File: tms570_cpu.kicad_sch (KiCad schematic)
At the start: 49 parts, among them J12 TS-103-G-A, J3 FTSH-105-01-L-DV-K, U2 TMS5700914APGEQQ1

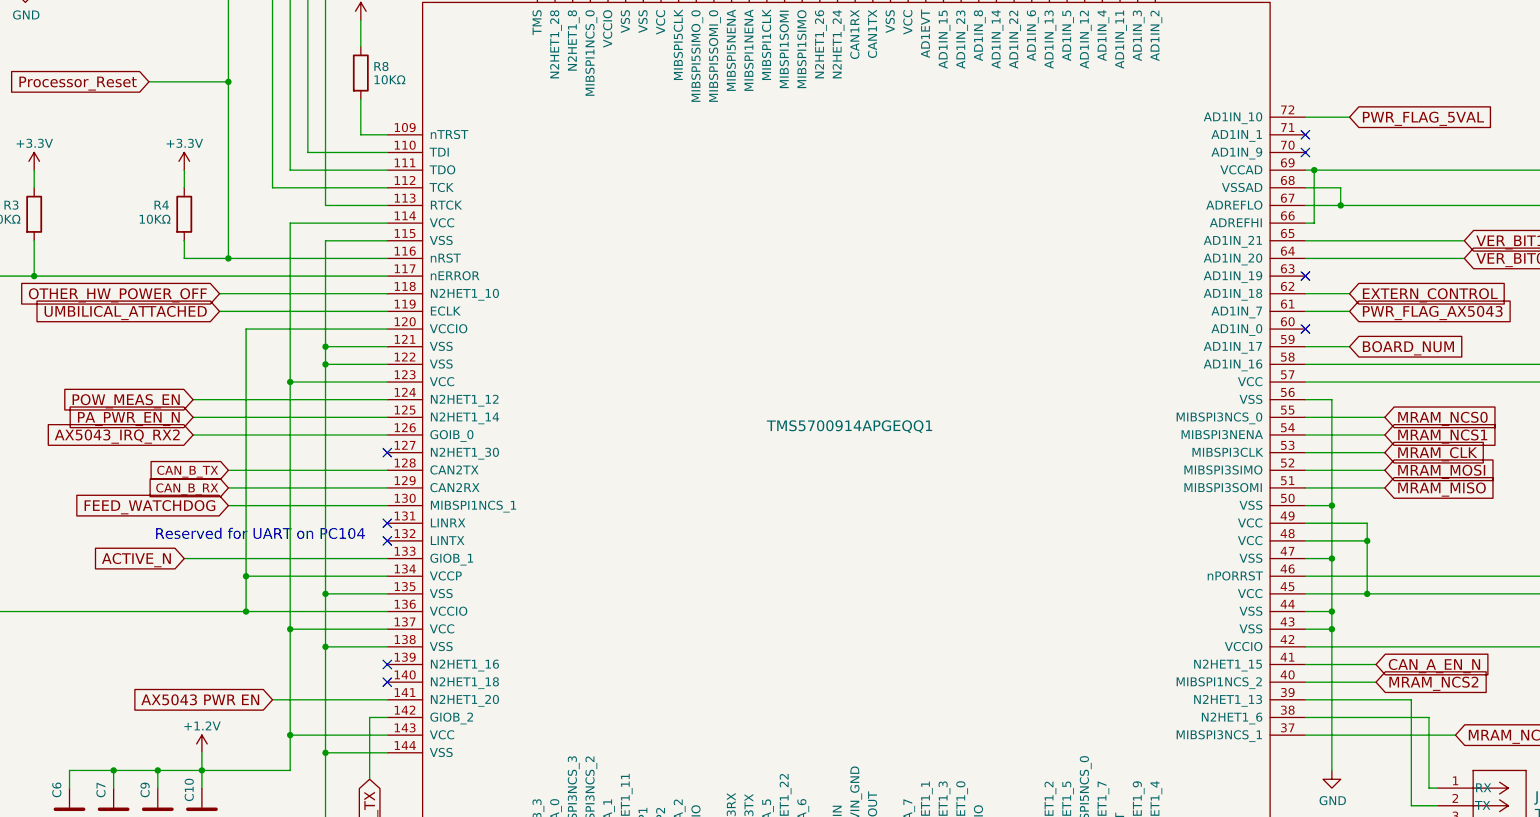
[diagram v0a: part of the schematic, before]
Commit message: Add some signals to the PC104
Add DNP zero-ohm resistors on the I2C lines to the PC104 so they can
be disconnected.

Add UART lines to the PC104 connected via DNP zero-ohm resistors.

Add a way to measure battery voltage from the PC104, currently with
DNP zero ohm resistors.

Signed-off-by: Corey Minyard <corey@minyard.net>
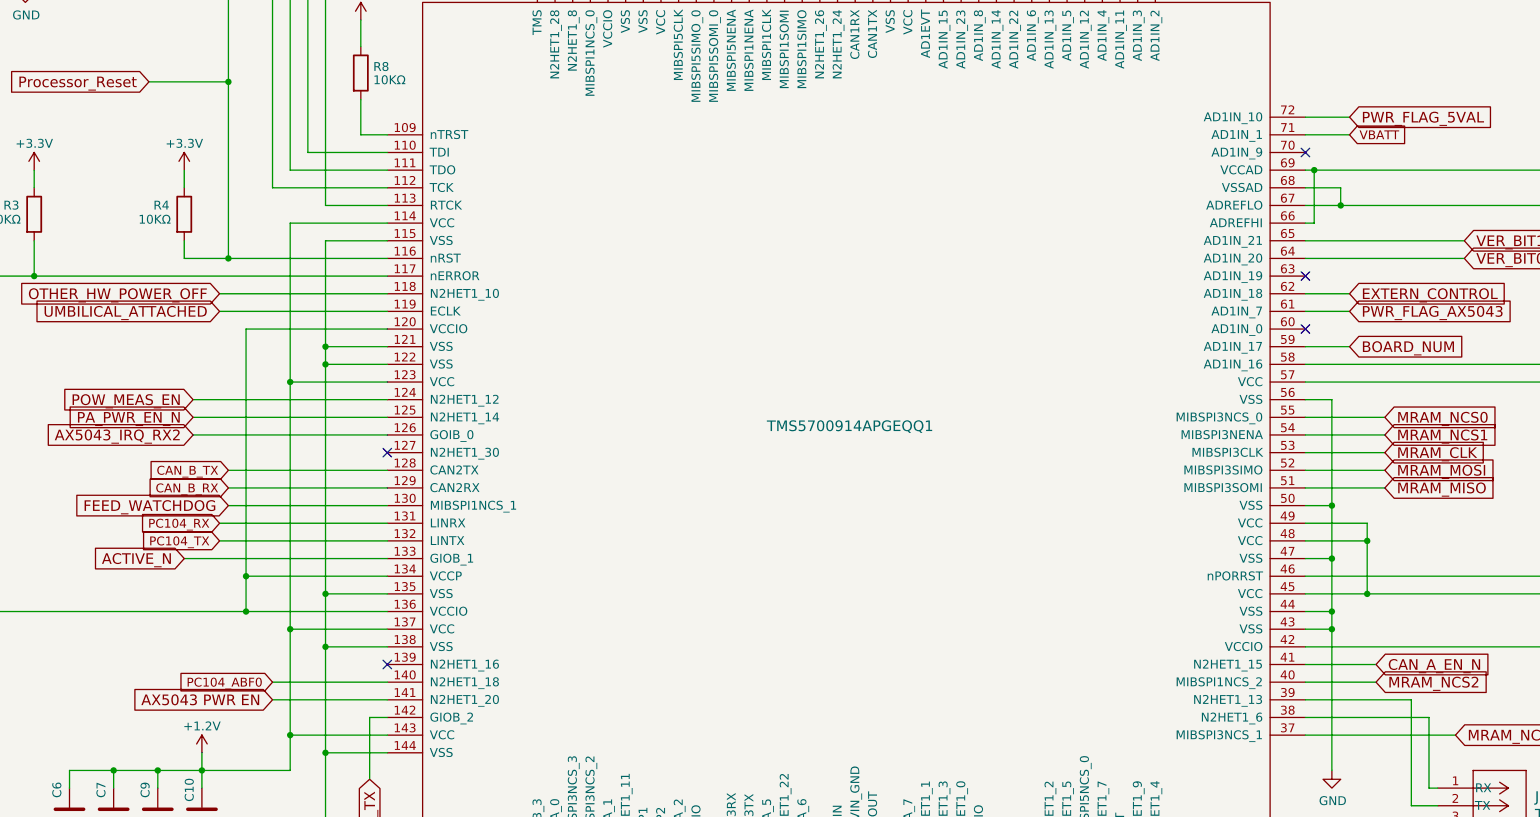
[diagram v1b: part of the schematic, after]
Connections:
- net PC104_RX: now reaches U2.131 (LINRX)
- net PC104_TX: now reaches U2.132 (LINTX)
- net PC104_ABF0: now reaches U2.140 (N2HET1_18)
- net VBATT: now reaches U2.71 (AD1IN_1)
- no-connect marks 22 -> 18
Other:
- note removed: "Reserved for UART on PC104"
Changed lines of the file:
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@@
 		)
 	)
-	(text "Reserved for UART on PC104"
-		(exclude_from_sim no)
-		(at 131.572 154.178 0)
-		(effects
-			(font
-				(size 1.524 1.524)
-			)
-		)
-	)
 	(text "Thermsistor varies from 534\nohms (125C) to 188.5KΩ (-40C).\nWith a 10KΩ bias this gives a\n.17 to 3.13V range."
 		(exclude_from_sim no)
@@
 	)
 	(no_connect
-		(at 281.94 96.52)
-	)
-	(no_connect
 		(at 281.94 124.46)
 	)
 	(no_connect
-		(at 149.86 154.94)
-	)
-	(no_connect
 		(at 196.85 72.39)
 	)
@@
 	)
 	(no_connect
-		(at 149.86 175.26)
-	)
-	(no_connect
-		(at 149.86 152.4)
-	)
-	(no_connect
 		(at 149.86 142.24)
 	)
@@
 	)
 	(no_connect
-		(at 281.94 99.06)
-	)
-	(no_connect
 		(at 191.77 72.39)
 	)
@@
 	)
 	(no_connect
+		(at 281.94 99.06)
+	)
+	(no_connect
 		(at 176.53 72.39)
 	)
@@
 	(wire
 		(pts
+			(xy 281.94 96.52) (xy 288.29 96.52)
+		)
+		(stroke
+			(width 0)
+			(type default)
+		)
+	)
+	(wire
+		(pts
 			(xy 254 38.1) (xy 254 39.37)
 		)
@@
 	(wire
 		(pts
+			(xy 125.73 154.94) (xy 149.86 154.94)
+		)
+		(stroke
+			(width 0)
+			(type default)
+		)
+	)
+	(wire
+		(pts
 			(xy 138.43 69.85) (xy 132.08 69.85)
 		)
@@
 	(wire
 		(pts
+			(xy 125.73 152.4) (xy 149.86 152.4)
+		)
+		(stroke
+			(width 0)
+			(type default)
+		)
+	)
+	(wire
+		(pts
 			(xy 113.03 217.17) (xy 113.03 222.25)
 		)
@@
 	(wire
 		(pts
+			(xy 133.35 175.26) (xy 149.86 175.26)
+		)
+		(stroke
+			(width 0)
+			(type default)
+		)
+	)
+	(wire
+		(pts
 			(xy 281.94 142.24) (xy 293.37 142.24)
 		)
@@
 		)
 	)
+	(global_label "VBATT"
+		(shape input)
+		(at 288.29 96.52 0)
+		(fields_autoplaced yes)
+		(effects
+			(font
+				(size 1.27 1.27)
+			)
+			(justify left)
+		)
+		(property "Intersheetrefs" "${INTERSHEET_REFS}"
+			(at 296.0034 96.52 0)
+			(effects
+				(font
+					(size 1.27 1.27)
+				)
+				(justify left)
+				(hide yes)
+			)
+		)
+	)
 	(global_label "MRAM_NCS1"
 		(shape input)
@@
 		)
 	)
+	(global_label "PC104_ABF0"
+		(shape input)
+		(at 133.35 175.26 180)
+		(fields_autoplaced yes)
+		(effects
+			(font
+				(size 1.27 1.27)
+			)
+			(justify right)
+		)
+		(property "Intersheetrefs" "${INTERSHEET_REFS}"
+			(at 119.2262 175.26 0)
+			(effects
+				(font
+					(size 1.27 1.27)
+				)
+				(justify right)
+				(hide yes)
+			)
+		)
+	)
 	(global_label "OTHER_ACTIVE_N"
 		(shape input)
@@
 		)
 	)
+	(global_label "PC104_RX"
+		(shape input)
+		(at 125.73 152.4 180)
+		(fields_autoplaced yes)
+		(effects
+			(font
+				(size 1.27 1.27)
+			)
+			(justify right)
+		)
+		(property "Intersheetrefs" "${INTERSHEET_REFS}"
+			(at 113.7834 152.4 0)
+			(effects
+				(font
+					(size 1.27 1.27)
+				)
+				(justify right)
+				(hide yes)
+			)
+		)
+	)
 	(global_label "OTHER_FAULT_N"
 		(shape input)
@@
 				(hide yes)
 			)
+		)
+	)
+	(global_label "PC104_TX"
+		(shape input)
+		(at 125.73 154.94 180)
+		(fields_autoplaced yes)
+		(effects
+			(font
+				(size 1.27 1.27)
+			)
+			(justify right)
+		)
+		(property "Intersheetrefs" "${INTERSHEET_REFS}"
+			(at 114.0858 154.94 0)
+			(effects
+				(font
+					(size 1.27 1.27)
+				)
+				(justify right)
+				(hide yes)
+			)

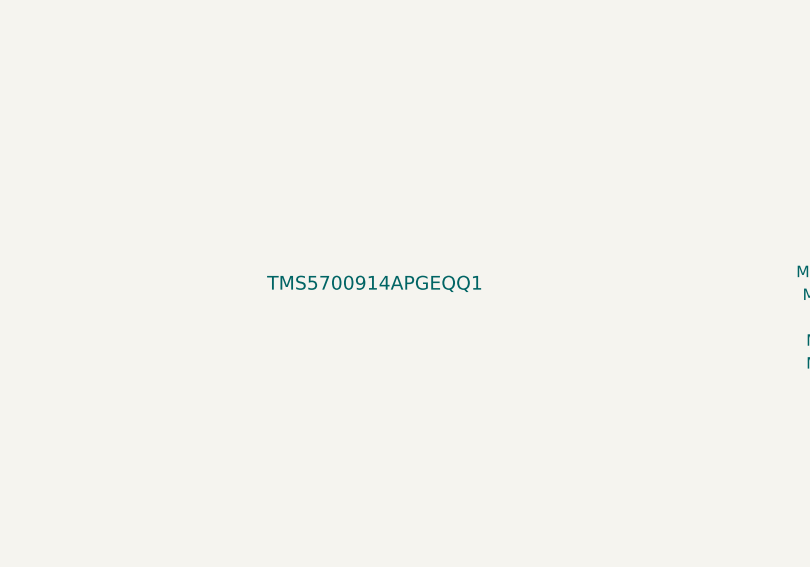
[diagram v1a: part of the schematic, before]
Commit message: Update schematics to match what is done to the boards so far
Get ready to split off a branch where the updates to the board can be
done while still keeping updates for the prototypes.

Signed-off-by: Corey Minyard <corey@minyard.net>
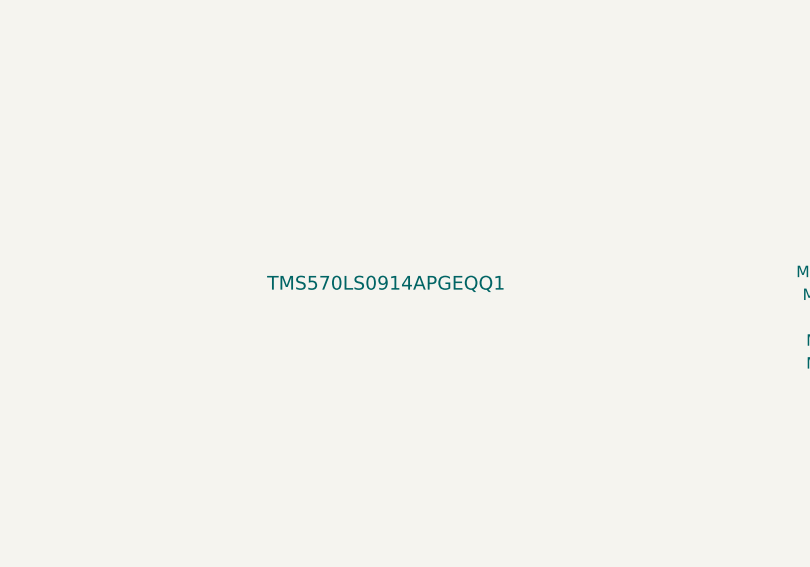
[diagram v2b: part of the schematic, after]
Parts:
- U2: value TMS5700914APGEQQ1 -> TMS570LS0914APGEQQ1
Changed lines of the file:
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@@
 			)
 		)
-		(property "Value" "TMS5700914APGEQQ1"
+		(property "Value" "TMS570LS0914APGEQQ1"
 			(at 204.47 138.43 0)
 			(effects

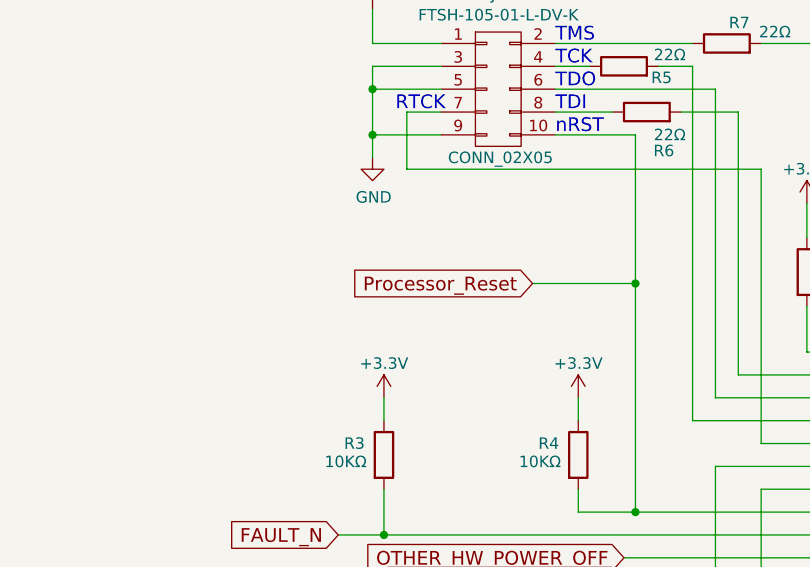
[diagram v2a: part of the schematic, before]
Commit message: Start doing PCB changes based on version 1 board
Signed-off-by: Corey Minyard <corey@minyard.net>
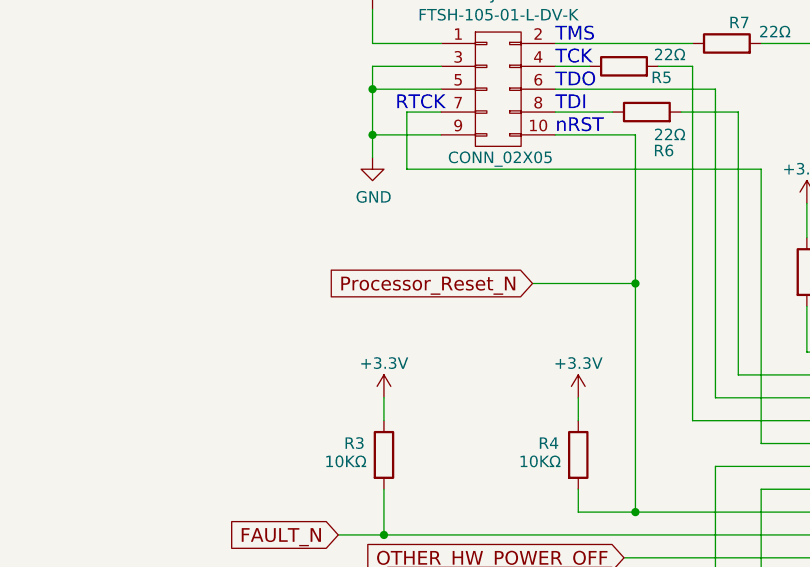
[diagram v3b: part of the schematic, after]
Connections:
- net Processor_Reset renamed Processor_Reset_N
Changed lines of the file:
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@@
 		)
 	)
-	(global_label "Processor_Reset"
+	(global_label "Processor_Reset_N"
 		(shape input)
 		(at 115.57 88.9 180)

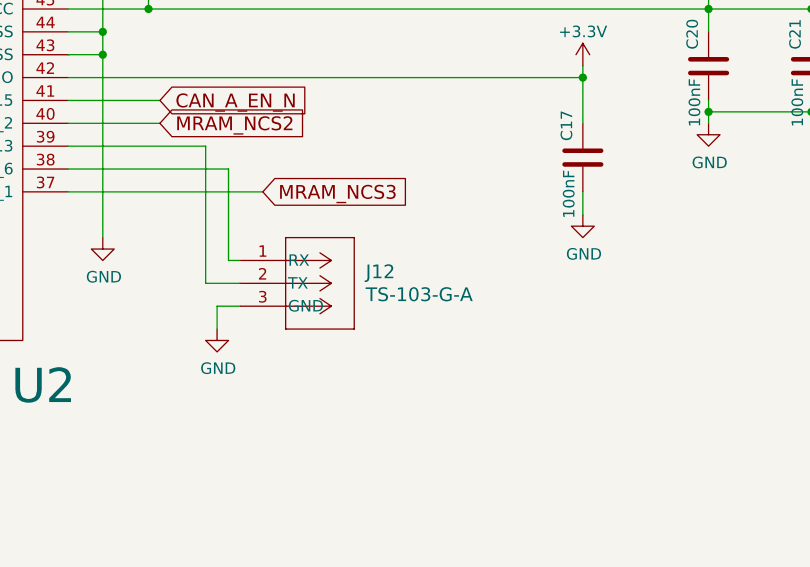
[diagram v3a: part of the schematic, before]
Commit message: More board reworks
Fix the MRAM part number.

Fix the power, voltags, and serial connectors.

Move the serial port connector so it doesn't conflict with the JTAG
port.

Add capacitor between the PA output L match and the filter to allow
easy separation for testing.

Signed-off-by: Corey Minyard <corey@minyard.net>
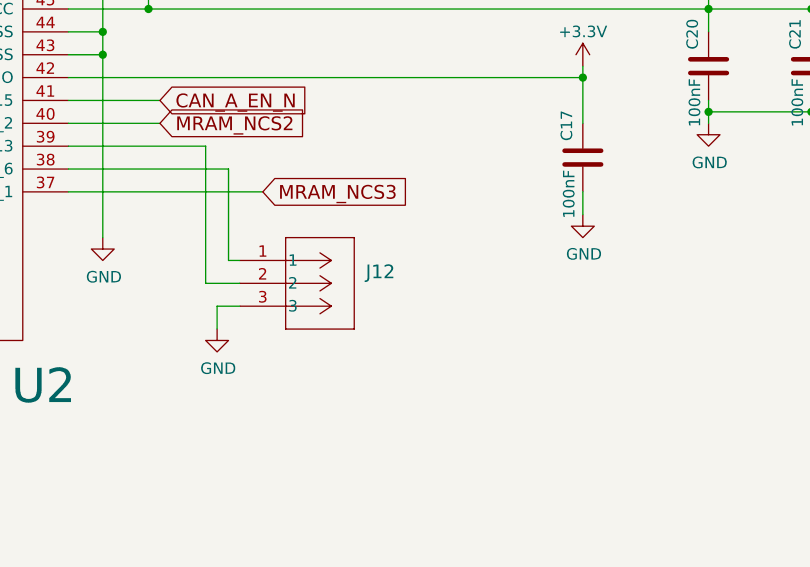
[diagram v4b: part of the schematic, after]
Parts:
- J12: value TS-103-G-A -> TSW-103-08-F-S-RA; footprint PacSatDev_misc:CON3_1X3_TU_HTS_SAI -> PacSatDev_misc:CON3_1X3_TR_TSW_SAI; symbol PACSAT_DEV_misc:TS-103-G-A_2-UART -> PACSAT_DEV_misc:TSW-103-08-F-S-RA
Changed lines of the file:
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@@
 	)
 	(symbol
-		(lib_id "PACSAT_DEV_misc:TS-103-G-A_2-UART")
+		(lib_id "PACSAT_DEV_misc:TSW-103-08-F-S-RA")
 		(at 300.99 190.5 0)
 		(unit 1)
@@
 			)
 		)
-		(property "Value" "TS-103-G-A"
+		(property "Value" "TSW-103-08-F-S-RA"
 			(at 314.96 194.3099 0)
 			(effects
@@
 				)
 				(justify left)
+				(hide yes)
 			)
 		)
-		(property "Footprint" "PacSatDev_misc:CON3_1X3_TU_HTS_SAI"
+		(property "Footprint" "PacSatDev_misc:CON3_1X3_TR_TSW_SAI"
 			(at 300.99 190.5 0)
 			(effects
@@
 			)
 		)
-		(property "Datasheet" "TS-103-G-A"
+		(property "Datasheet" "TSW-103-08-F-S-RA"
 			(at 300.99 190.5 0)
 			(effects

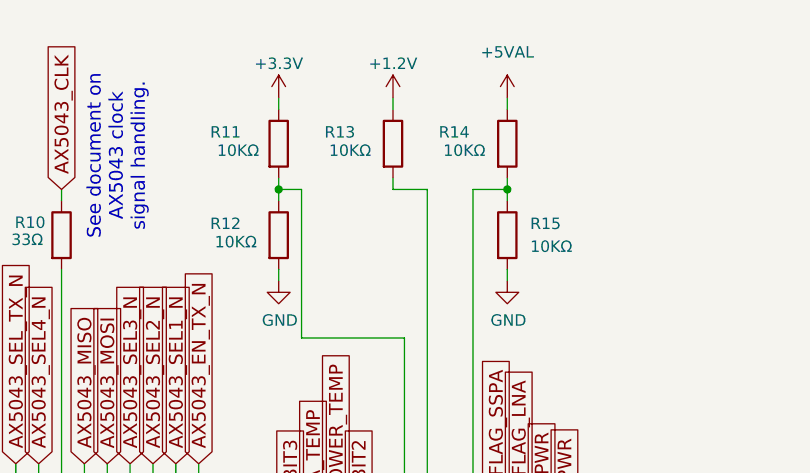
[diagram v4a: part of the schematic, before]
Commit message: Change power measurement resistors to 1%
Also do some part fixes.

Signed-off-by: Corey Minyard <corey@minyard.net>
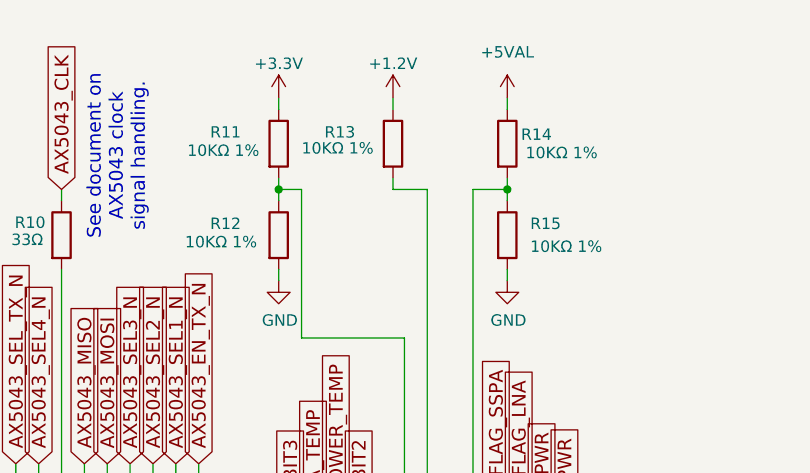
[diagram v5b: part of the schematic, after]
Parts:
- R11, R12, R13, R14, R15: value 10KΩ -> 10KΩ 1%
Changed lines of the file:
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@@
 			)
 		)
-		(property "Value" "10KΩ"
-			(at 234.188 24.892 0)
+		(property "Value" "10KΩ 1%"
+			(at 231.14 24.638 0)
 			(effects
 				(font
@@
 		(dnp no)
 		(property "Reference" "R14"
-			(at 246.38 22.86 0)
+			(at 255.524 23.114 0)
 			(effects
 				(font
@@
 			)
 		)
-		(property "Value" "10KΩ"
-			(at 246.888 24.892 0)
+		(property "Value" "10KΩ 1%"
+			(at 256.032 25.146 0)
 			(effects
 				(font
@@
 			)
 		)
-		(property "Value" "10KΩ"
+		(property "Value" "10KΩ 1%"
 			(at 256.54 35.56 0)
 			(effects
@@
 			)
 		)
-		(property "Value" "10KΩ"
-			(at 221.488 35.052 0)
+		(property "Value" "10KΩ 1%"
+			(at 218.186 35.052 0)
 			(effects
 				(font
@@
 			)
 		)
-		(property "Value" "10KΩ"
-			(at 221.742 24.892 0)
-			(effects
-				(font
+		(property "Value" "10KΩ 1%"
+			(at 218.44 24.892 0)
+			(effects
+				(font

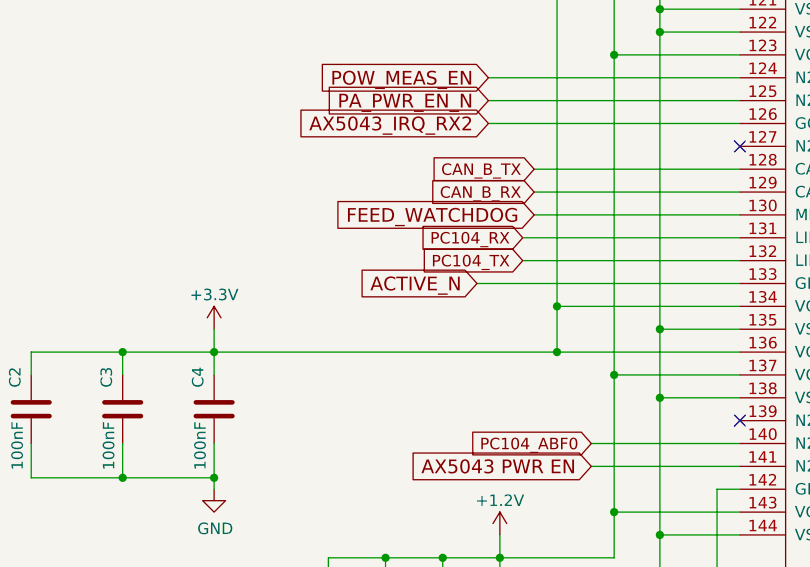
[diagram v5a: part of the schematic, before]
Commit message: Fix a reset issue with ACTIVE_N
Like the OTHER_HW_POWER_OFF_N in a previous commit, the ACTIVE_N line
was pulled low when the CPU was in reset, which could mess up fault
tolerance because ACTIVE1 controls the RF output switch.  Add a
transistor there and switch it to positive logic, ACTIVE instead.  FAULT
doesn't seem to have the issue and the rest of the lines shouldn't
matter as they are only outputs from the other board.

Signed-off-by: Corey Minyard <corey@minyard.net>
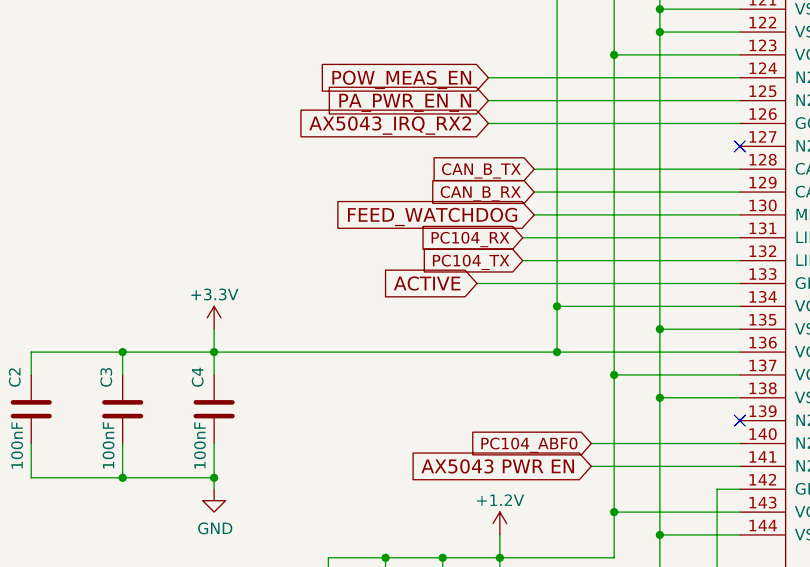
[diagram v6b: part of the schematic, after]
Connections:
- net ACTIVE_N renamed ACTIVE
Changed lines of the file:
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@@
 		)
 	)
-	(global_label "ACTIVE_N"
+	(global_label "ACTIVE"
 		(shape input)
 		(at 120.65 157.48 180)
